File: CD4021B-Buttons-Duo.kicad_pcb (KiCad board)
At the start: 2 copper layers, 100 x 50 mm, 50 parts, among them J1 2.54, J10 JST XH, J11 JST XH, J12 JST XH, J13 JST XH, J14 JST XH, J15 JST XH, J16 JST XH, J17 JST XH, J18 3.5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

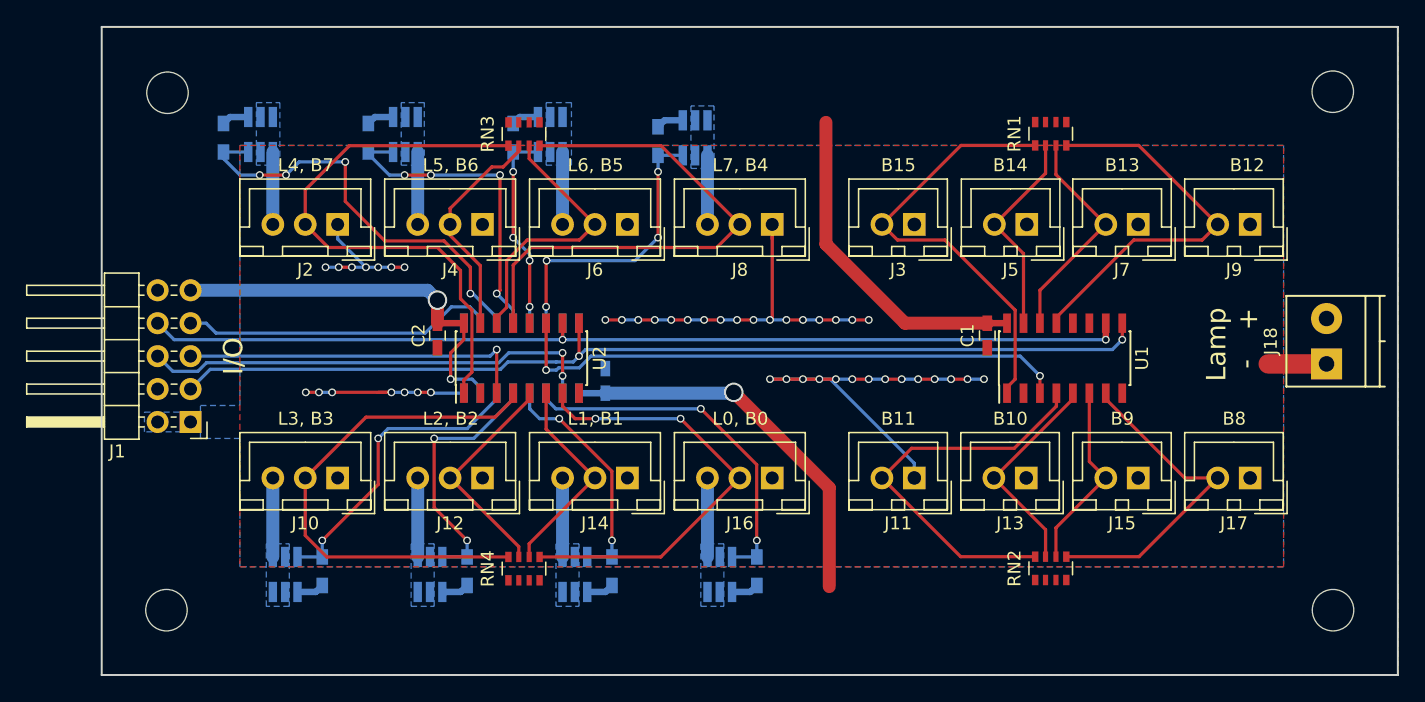
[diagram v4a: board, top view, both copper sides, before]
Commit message: Attempt to optimize connections for bypass capacitors
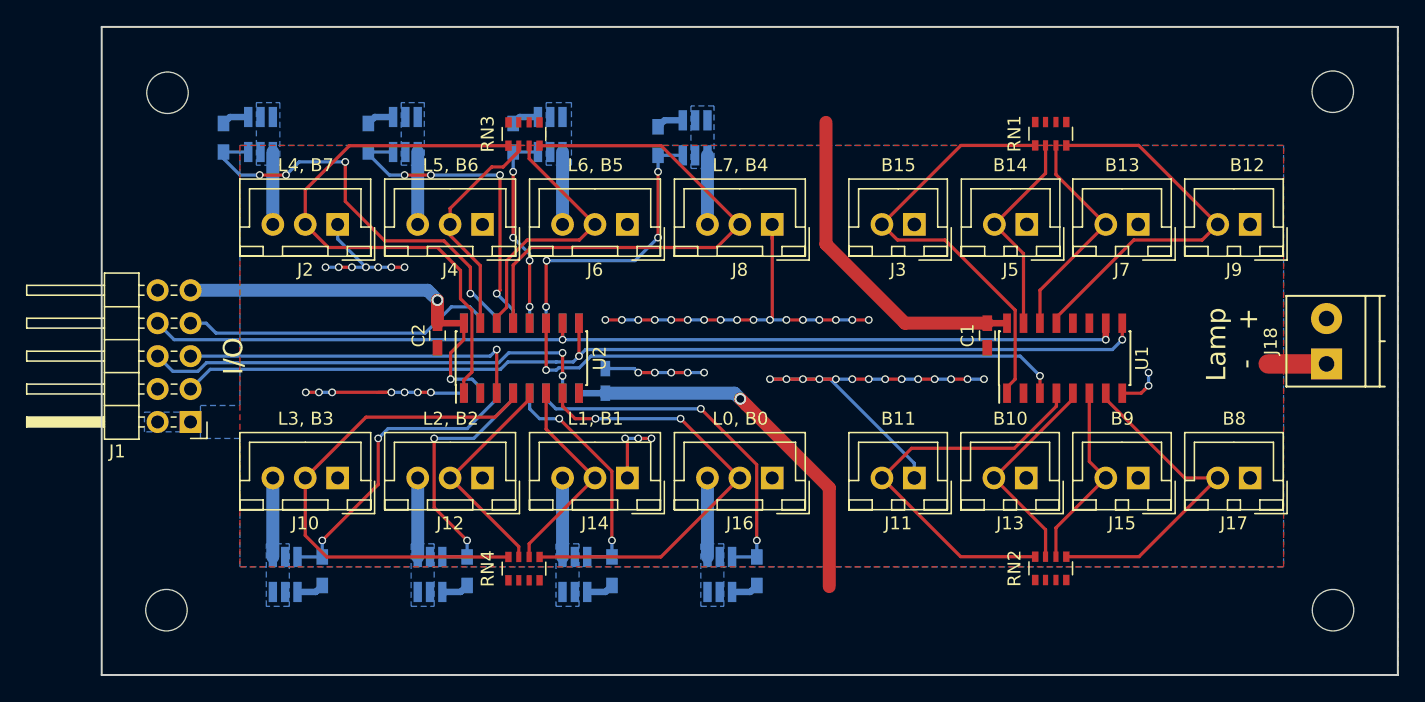
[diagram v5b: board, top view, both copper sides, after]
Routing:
- net GND: track 88.4 -> 104.6 mm, vias 45 -> 55
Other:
- net class LocalPower: via_dia 1.5 -> 0.9; via_drill 1.2 -> 0.6
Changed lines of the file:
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@@
     (links 155)
     (no_connects 0)
-    (area 97.329048 78.918999 213.490953 129.069001)
+    (area 105.334999 78.918999 205.485001 129.069001)
     (thickness 1.6)
     (drawings 28)
-    (tracks 400)
+    (tracks 427)
     (zones 0)
     (modules 50)
@@
     (clearance 0.2)
     (trace_width 1)
-    (via_dia 1.5)
-    (via_drill 1.2)
+    (via_dia 0.9)
+    (via_drill 0.6)
     (uvia_dia 0.3)
     (uvia_drill 0.1)
@@
   (gr_line (start 205.41 78.994) (end 205.41 128.994) (layer Edge.Cuts) (width 0.15))
   (gr_line (start 105.41 78.994) (end 205.41 78.994) (layer Edge.Cuts) (width 0.15))
-  (segment (start 154.1145 107.2515) (end 154.178 107.188) (width 1) (layer B.Cu) (net 1))
-  (segment (start 144.272 107.2515) (end 154.1145 107.2515) (width 1) (layer B.Cu) (net 1) (status 10))
-  (segment (start 161.544 114.554) (end 154.178 107.188) (width 1) (layer F.Cu) (net 1))
-  (segment (start 161.544 122.174) (end 161.544 114.554) (width 1) (layer F.Cu) (net 1))
-  (via (at 154.178 107.188) (size 1.5) (drill 1.2) (layers F.Cu B.Cu) (net 1))
+  (segment (start 155.135999 108.146001) (end 154.686 107.696002) (width 1) (layer F.Cu) (net 1))
+  (segment (start 161.544 114.554002) (end 155.135999 108.146001) (width 1) (layer F.Cu) (net 1))
+  (segment (start 161.544 122.174) (end 161.544 114.554002) (width 1) (layer F.Cu) (net 1))
+  (segment (start 154.241498 107.2515) (end 154.686 107.696002) (width 1) (layer B.Cu) (net 1))
+  (segment (start 144.272 107.2515) (end 154.241498 107.2515) (width 1) (layer B.Cu) (net 1))
+  (via (at 154.686 107.696002) (size 0.9) (drill 0.6) (layers F.Cu B.Cu) (net 1))
+  (segment (start 130.868001 99.625991) (end 131.318 100.07599) (width 1) (layer B.Cu) (net 1))
+  (segment (start 130.55601 99.314) (end 130.868001 99.625991) (width 1) (layer B.Cu) (net 1))
+  (segment (start 112.268 99.314) (end 130.55601 99.314) (width 1) (layer B.Cu) (net 1))
+  (segment (start 131.318 101.854) (end 131.318 100.07599) (width 1) (layer F.Cu) (net 1))
+  (via (at 131.318 100.07599) (size 0.9) (drill 0.6) (layers F.Cu B.Cu) (net 1))
   (segment (start 142.24 107.254) (end 144.2695 107.254) (width 0.5) (layer B.Cu) (net 1) (status 30))
   (segment (start 144.2695 107.254) (end 144.272 107.2515) (width 0.5) (layer B.Cu) (net 1) (status 30))
@@
   (segment (start 167.386 101.854) (end 161.29 95.758) (width 1) (layer F.Cu) (net 1))
   (segment (start 161.29 95.758) (end 161.29 86.36) (width 1) (layer F.Cu) (net 1))
-  (segment (start 130.556 99.314) (end 131.318 100.076) (width 1) (layer B.Cu) (net 1))
-  (segment (start 112.268 99.314) (end 130.556 99.314) (width 1) (layer B.Cu) (net 1) (status 10))
-  (via (at 131.318 100.076) (size 1.5) (drill 1.2) (layers F.Cu B.Cu) (net 1))
-  (segment (start 131.318 101.854) (end 131.318 100.076) (width 1) (layer F.Cu) (net 1) (status 10))
   (segment (start 131.318 101.854) (end 133.35 101.854) (width 0.5) (layer F.Cu) (net 1) (status 30))
+  (segment (start 150.621986 105.664) (end 149.352 105.664) (width 0.25) (layer F.Cu) (net 2))
+  (segment (start 148.081994 105.664) (end 149.352 105.664) (width 0.25) (layer B.Cu) (net 2))
+  (via (at 149.352 105.664) (size 0.6) (drill 0.4) (layers F.Cu B.Cu) (net 2))
+  (segment (start 151.892 105.664) (end 150.621986 105.664) (width 0.25) (layer B.Cu) (net 2))
+  (via (at 150.621986 105.664) (size 0.6) (drill 0.4) (layers F.Cu B.Cu) (net 2))
+  (via (at 151.892 105.664) (size 0.6) (drill 0.4) (layers F.Cu B.Cu) (net 2))
+  (segment (start 146.812 105.664) (end 148.081994 105.664) (width 0.25) (layer F.Cu) (net 2))
+  (via (at 148.081994 105.664) (size 0.6) (drill 0.4) (layers F.Cu B.Cu) (net 2))
+  (segment (start 146.4995 105.3515) (end 146.512001 105.364001) (width 0.25) (layer B.Cu) (net 2))
+  (segment (start 144.272 105.3515) (end 146.4995 105.3515) (width 0.25) (layer B.Cu) (net 2))
+  (segment (start 146.512001 105.364001) (end 146.812 105.664) (width 0.25) (layer B.Cu) (net 2))
+  (via (at 146.812 105.664) (size 0.6) (drill 0.4) (layers F.Cu B.Cu) (net 2))
+  (segment (start 186.182 106.68) (end 186.182 105.664) (width 0.25) (layer B.Cu) (net 2))
+  (via (at 186.182 105.664) (size 0.6) (drill 0.4) (layers F.Cu B.Cu) (net 2))
+  (segment (start 185.882001 106.979999) (end 186.182 106.68) (width 0.25) (layer F.Cu) (net 2))
+  (segment (start 185.608 107.254) (end 185.882001 106.979999) (width 0.25) (layer F.Cu) (net 2))
+  (segment (start 184.15 107.254) (end 185.608 107.254) (width 0.25) (layer F.Cu) (net 2))
+  (via (at 186.182 106.68) (size 0.6) (drill 0.4) (layers F.Cu B.Cu) (net 2))
+  (segment (start 146.812 110.744) (end 147.828 110.744) (width 0.25) (layer F.Cu) (net 2))
+  (via (at 147.828 110.744) (size 0.6) (drill 0.4) (layers F.Cu B.Cu) (net 2))
+  (segment (start 145.796 110.744) (end 146.812 110.744) (width 0.25) (layer B.Cu) (net 2))
+  (via (at 146.812 110.744) (size 0.6) (drill 0.4) (layers F.Cu B.Cu) (net 2))
+  (segment (start 145.97 113.792) (end 145.97 110.918) (width 0.25) (layer F.Cu) (net 2))
+  (segment (start 145.97 110.918) (end 145.796 110.744) (width 0.25) (layer F.Cu) (net 2))
+  (via (at 145.796 110.744) (size 0.6) (drill 0.4) (layers F.Cu B.Cu) (net 2))
   (segment (start 199.91 104.994) (end 195.41 104.994) (width 1.5) (layer F.Cu) (net 2) (status 10))
   (segment (start 122.174 107.188) (end 121.158 107.188) (width 0.25) (layer F.Cu) (net 2))

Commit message: Cosmetic
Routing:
- net /CHAIN: track 44.1 -> 45.0 mm

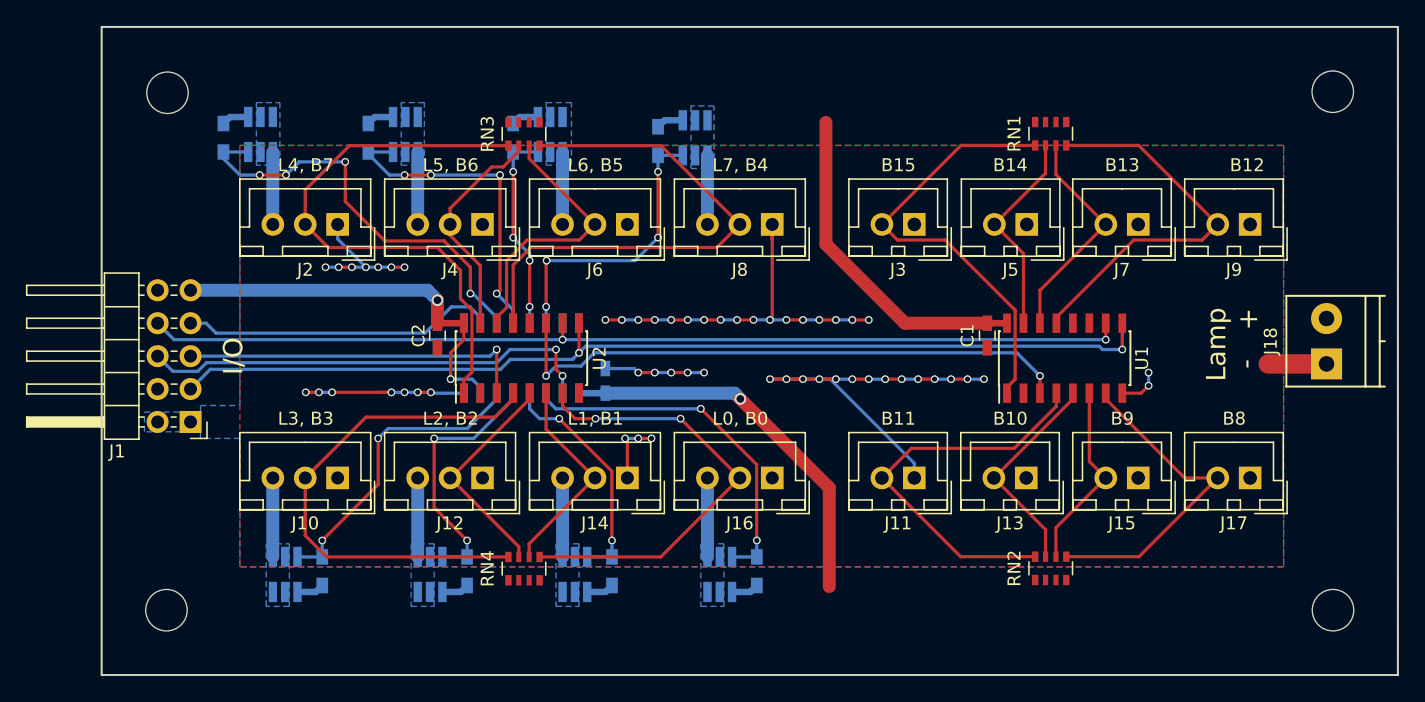
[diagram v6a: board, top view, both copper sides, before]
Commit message: Adjust traces
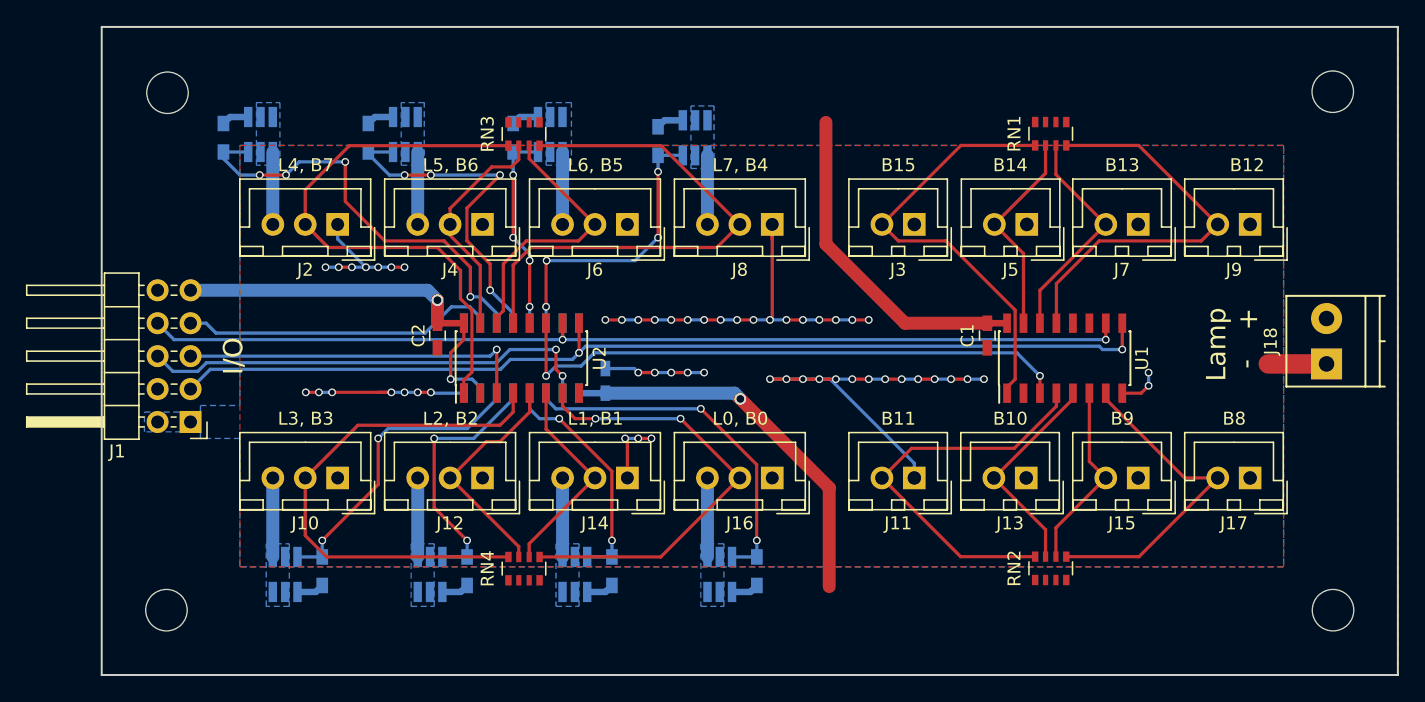
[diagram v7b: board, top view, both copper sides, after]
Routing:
- net /LD6: track 25.0 -> 27.8 mm
- net /D12: track 30.1 -> 31.6 mm
- net /D2: track 17.4 -> 18.0 mm
- net /D3: track 39.8 -> 40.4 mm
